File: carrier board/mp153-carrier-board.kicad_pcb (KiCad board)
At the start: 4 copper layers, 66 x 75 mm, 27 parts, among them J3 USB_B_Micro_10118194-0011LF, J4 Socket_02x40_P0.4mm_W3.0mm_SMT, J5 3.5mm_Mono_Switched_sm, J6 Socket_02x40_P0.4mm_W3.0mm_SMT, J7 Eurorack_Power_16pin_Unshroud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, J9 3.5mm_Mono_Switched_sm, U1 TL072H

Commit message: Carrier-board: Added codec and audio in/out
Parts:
- removed J3: USB_B_Micro_10118194-0011LF, Connector_USB:USB_Micro-B_Amphenol_10118194_Horizontal
- added C147: 180pF_0402_25V, 4ms_Capacitor:C_0402, B.Cu at (224.3, 78.4)
- added C148: 180pF_0402_25V, 4ms_Capacitor:C_0402, B.Cu at (229.0, 84.0)
- added C149: 180pF_0402_25V, 4ms_Capacitor:C_0402, B.Cu at (227.2, 74.5)
- added C150: 180pF_0402_25V, 4ms_Capacitor:C_0402, B.Cu at (231.9, 77.4)
- added C152: 820pF_0402_10v, 4ms_Capacitor:C_0402, B.Cu at (226.0, 84.1)
- added C153: 820pF_0402_10v, 4ms_Capacitor:C_0402, B.Cu at (230.1, 73.5)
- added C41: 100nF_0402_16V, 4ms_Capacitor:C_0402, F.Cu at (216.9, 64.9)
- added C42: 220pF_0603_25V, 4ms_Capacitor:C_0603, B.Cu at (217.7, 75.3)
- added C44: 22uF_0805_10V, 4ms_Capacitor:C_0805, F.Cu at (216.1, 67.5)
- added C45: 0.1uF_0603_16V, 4ms_Capacitor:C_0603, F.Cu at (216.1, 69.2)
- added C46: 2.2uF_0603_25V, 4ms_Capacitor:C_0603, B.Cu at (214.7, 82.9)
- added C48: 220pF_0603_25V, 4ms_Capacitor:C_0603, B.Cu at (210.3, 75.9)
- added C49: 2.2uF_0603_25V, 4ms_Capacitor:C_0603, B.Cu at (223.8, 69.4)
- added C51: 10uF_0603_10V, 4ms_Capacitor:C_0603, B.Cu at (223.8, 64.2)
- added C52: 2.2uF_0603_25V, 4ms_Capacitor:C_0603, B.Cu at (212.7, 76.9)
- added C71: 100nF_0402_50V, 4ms_Capacitor:C_0402, B.Cu at (219.9, 79.7)
- added C72: 100nF_0402_50V, 4ms_Capacitor:C_0402, B.Cu at (220.0, 81.7)
- added C75: 100nF_0402_50V, 4ms_Capacitor:C_0402, B.Cu at (212.4, 79.5)
- added C76: 100nF_0402_50V, 4ms_Capacitor:C_0402, B.Cu at (212.4, 82.2)
- added C77: 100nF_0402_50V, 4ms_Capacitor:C_0402, B.Cu at (229.8, 80.5)
- added C78: 100nF_0402_50V, 4ms_Capacitor:C_0402, B.Cu at (229.7, 78.5)
- added J1: USB-C_Receptacle_Molex_2171790001, 4ms_Connector:USB_C_Receptacle_Molex_2171790001, B.Cu at (222.5, 45.6)
- added NT1: NetTie_2, NetTie:NetTie-2_SMD_Pad0.5mm, B.Cu at (224.4, 62.8)
- added R10: 10k_0402, 4ms_Resistor:R_0402, B.Cu at (224.3, 76.2)
- added R14: 10k_0402, 4ms_Resistor:R_0402, B.Cu at (224.4, 77.2)
- added R152: 1k_0402, 4ms_Resistor:R_0402, B.Cu at (224.3, 79.5)
- added R153: 1k_0402, 4ms_Resistor:R_0402, B.Cu at (225.6, 74.1)
- added R157: 24k_0402, 4ms_Resistor:R_0402, B.Cu at (224.3, 80.7)
- added R158: 10k_0402, 4ms_Resistor:R_0402, B.Cu at (227.0, 84.1)
- added R159: 10k_0402, 4ms_Resistor:R_0402, B.Cu at (228.0, 84.0)
- added R160: 24k_0402, 4ms_Resistor:R_0402, B.Cu at (224.4, 84.0)
- added R161: 24k_0402, 4ms_Resistor:R_0402, B.Cu at (227.2, 73.5)
- added R162: 10k_0402, 4ms_Resistor:R_0402, B.Cu at (228.6, 74.1)
- added R163: 10k_0402, 4ms_Resistor:R_0402, B.Cu at (229.7, 76.1)
- added R164: 24k_0402, 4ms_Resistor:R_0402, B.Cu at (230.9, 77.4)
- added R3: 5.1k_0603, 4ms_Resistor:R_0603, F.Cu at (237.5, 83.7)
- added R4: 5.1k_0603, 4ms_Resistor:R_0603, F.Cu at (237.5, 86.2)
- added R42: 14k_0402, 4ms_Resistor:R_0402, B.Cu at (217.1, 74.0)
- added R43: 100k_0402, 4ms_Resistor:R_0402, B.Cu at (215.0, 78.4)
- added R44: 1k_0402, 4ms_Resistor:R_0402, B.Cu at (218.5, 84.7)
- added R47: 4.7k_0402, 4ms_Resistor:R_0402, B.Cu at (210.7, 60.3)
- added R48: 4.7k_0402, 4ms_Resistor:R_0402, B.Cu at (210.7, 59.2)
- added R49: 1M_0402, 4ms_Resistor:R_0402, B.Cu at (216.6, 84.7)
- added R50: 14k_0402, 4ms_Resistor:R_0402, B.Cu at (210.3, 74.5)
- added R51: 100k_0402, 4ms_Resistor:R_0402, B.Cu at (210.2, 73.3)
- added R52: 1k_0402, 4ms_Resistor:R_0402, B.Cu at (211.0, 85.4)
- added R53: 1M_0402, 4ms_Resistor:R_0402, B.Cu at (209.0, 85.4)
- added R54: 1k_0402, 4ms_Resistor:R_0402, B.Cu at (212.2, 73.2)
- added R55: 1k_0402, 4ms_Resistor:R_0402, B.Cu at (217.1, 72.9)
- added R6: 10k_0402, 4ms_Resistor:R_0402, B.Cu at (224.3, 81.9)
- added R7: 10k_0402, 4ms_Resistor:R_0402, B.Cu at (224.3, 83.0)
- added U11: NJM2068, 4ms_Package_SSOP:TSSOP-8_4.4x3mm_Pitch0.65mm, B.Cu at (210.0, 80.7)
- added U12: NJM2068, 4ms_Package_SSOP:TSSOP-8_4.4x3mm_Pitch0.65mm, B.Cu at (227.3, 79.1)
- added U8: NJM2068, 4ms_Package_SSOP:TSSOP-8_4.4x3mm_Pitch0.65mm, B.Cu at (217.4, 80.2)
- added U9: PCM3060PW, Package_SO:TSSOP-28_4.4x9.7mm_P0.65mm, B.Cu at (216.9, 66.1)
- added V1: AP2120N-5.0TRG1, 4ms_Package_SOT:SOT23-3_PO132, B.Cu at (224.1, 66.8)
- renumbered R6 to R8
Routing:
- net GND: track 0.00 -> 125.4 mm, vias 0 -> 15
- net -12VA: track 0.00 -> 36.3 mm, vias 0 -> 5
- net +12V: track 0.00 -> 32.1 mm, vias 0 -> 5
- net +3V3: track 0.00 -> 28.6 mm, vias 0 -> 3
- net GNDA: track 0.00 -> 22.4 mm, vias 0 -> 2
- net /VCOM: track 0.00 -> 21.4 mm, vias 0 -> 5
- net /SAI_FS: track 0.00 -> 20.4 mm, vias 0 -> 1
- net /SAI_SCK: track 0.00 -> 19.5 mm, vias 0 -> 1
- net /SAI_MCLK: track 0.00 -> 17.3 mm, vias 0 -> 1
- net /CODEC_OUT_L+: track 0.00 -> 16.7 mm
- net /CODEC_OUT_L-: track 0.00 -> 16.1 mm
- net /SAI_SD_B: track 0.00 -> 15.7 mm, vias 0 -> 1
- net /D10: track 0.00 -> 15.5 mm, vias 0 -> 1
- net /D17: track 0.00 -> 14.0 mm, vias 0 -> 1
- net /SAI_SD_A: track 0.00 -> 13.6 mm, vias 0 -> 1
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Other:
- board size 66 x 75 mm -> 66 x 78 mm

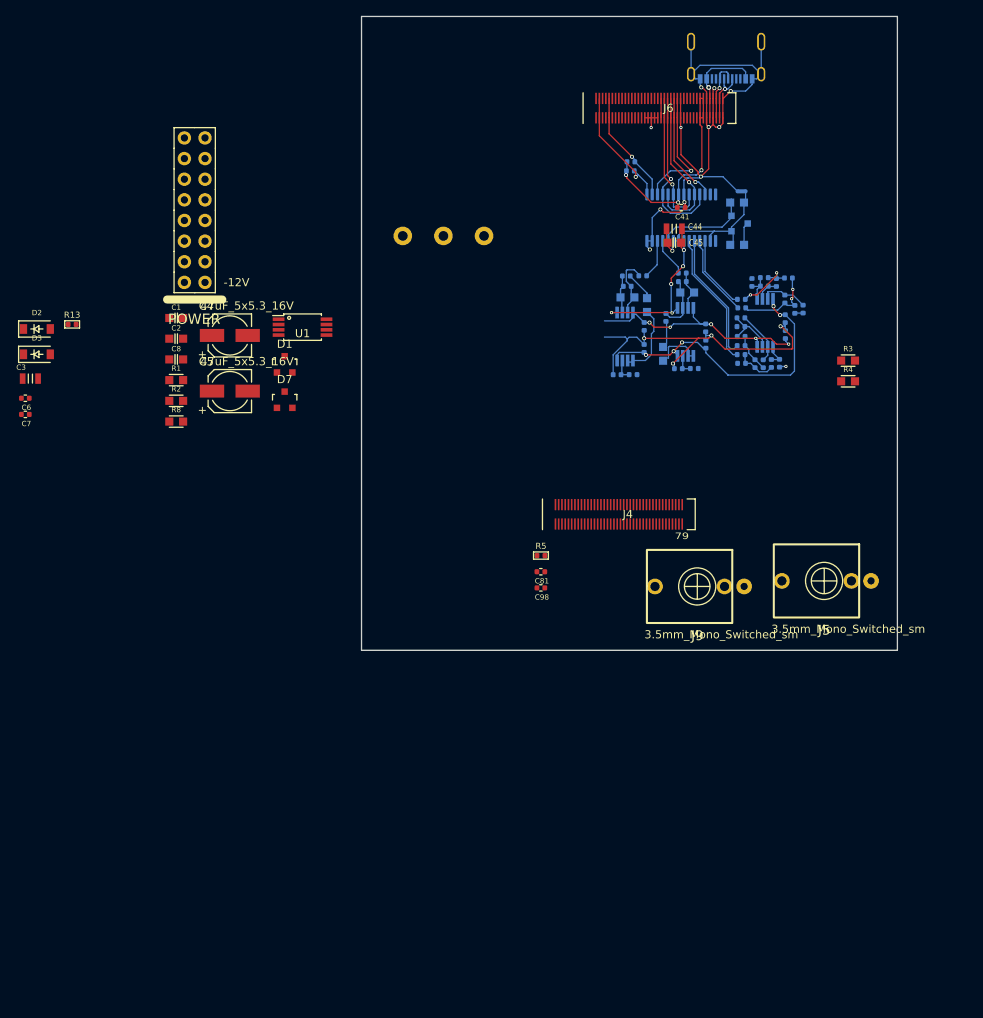
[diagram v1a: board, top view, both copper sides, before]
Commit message: Finished carrier board. Produced JLC files
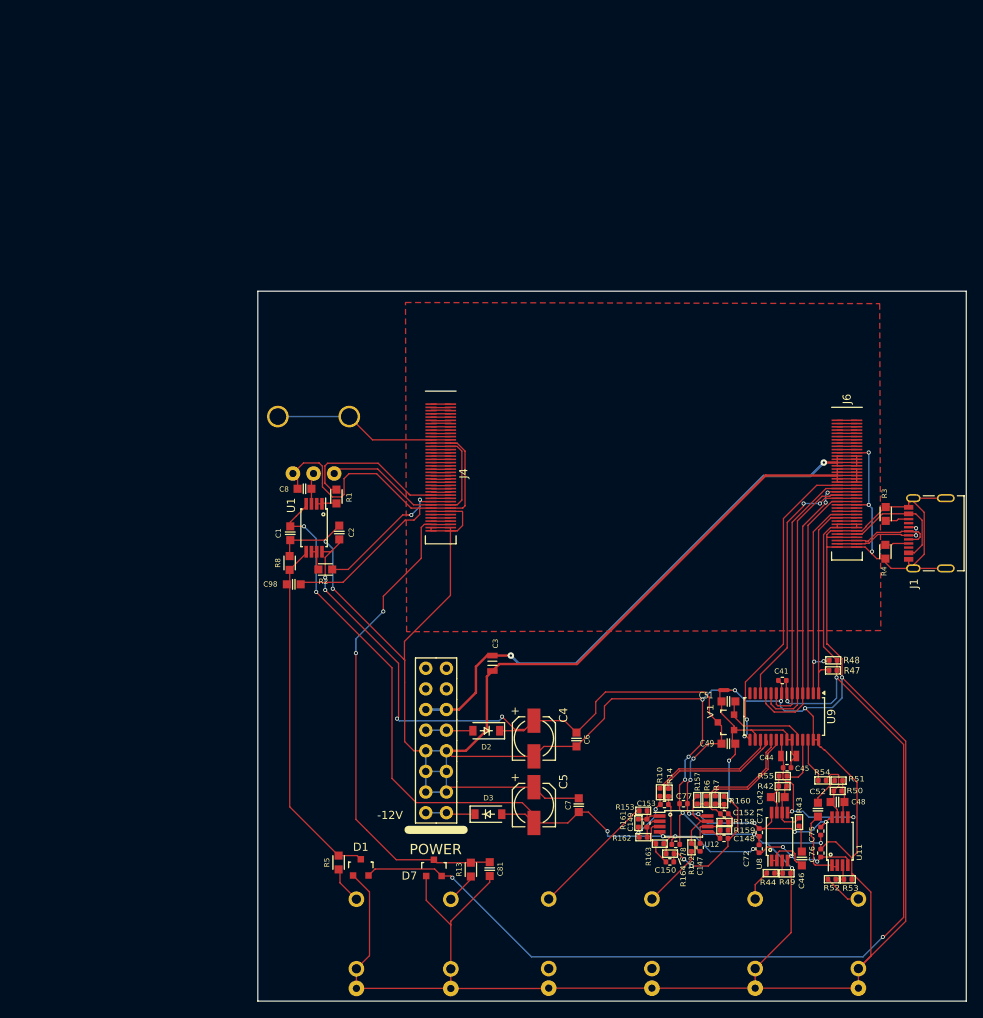
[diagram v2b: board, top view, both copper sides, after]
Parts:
- added J10: 3.5mm_Mono_Switched_sm, 4ms_Jack:EighthInch_PJ398SM, B.Cu at (226.0, 155.2)
- added J11: 3.5mm_Mono_Switched_sm, 4ms_Jack:EighthInch_PJ398SM, B.Cu at (238.7, 155.2)
- added J12: 3.5mm_Mono_Switched_sm, 4ms_Jack:EighthInch_PJ398SM, B.Cu at (200.6, 155.2)
- added J13: 3.5mm_Mono_Switched_sm, 4ms_Jack:EighthInch_PJ398SM, B.Cu at (213.3, 155.2)
- C147, C148, C149, C150, C152, C153, C42, C46, C48, C49, C51, C52, C71, C72, C75, C76, C77, C78, J1, NT1, R10, R14, R152, R153, R157, R158, R159, R160, R161, R162, R163, R164, R42, R43, R44, R47, R48, R49, R50, R51, R52, R53, R54, R55, R6, R7, U9, V1: moved to F.Cu
- C44: value 22uF_0805_10V -> 22uF_0805_25V
- C45: value 0.1uF_0603_16V -> 100nF_0402_16V; footprint 4ms_Capacitor:C_0603 -> 4ms_Capacitor:C_0402
- C6, C7: value 100nF_0402_16V -> 100nF_0603_16V; footprint 4ms_Capacitor:C_0402 -> 4ms_Capacitor:C_0603
- C81, C98: value 10nF_0402_16V -> 10nF_0603_25V; footprint 4ms_Capacitor:C_0402 -> 4ms_Capacitor:C_0603
- J5, J9: moved to B.Cu
- POT1: value 16mm_CtrDet_10k -> 9mm_NoDet_100k_Knurled_Lined; footprint 4ms_Potentiometer:Pot_16mm_CtrDet_RV16AF-4A -> 4ms_Potentiometer:Pot_9mm_Knurl_NoDet
- R1, R2: value 68R_0603 -> 68Ω_0603
- R13, R5: value 47k_0402 -> 47k_0603; footprint 4ms_Resistor:R_0402 -> 4ms_Resistor:R_0603
- U11, U12, U8: value NJM2068 -> TL072H; moved to F.Cu
- moved C7 83.4 mm to (204.3, 138.4), turned to 90 degrees
- moved R13 83.1 mm to (191.0, 146.3), turned to 90 degrees
- moved C6 79.8 mm to (204.0, 130.3), turned to -90 degrees
- moved D3 79.3 mm to (193.2, 139.5)
- moved D2 74.2 mm to (192.9, 129.2), turned to 180 degrees
- moved J5 72.7 mm to (176.9, 155.2), turned to -90 degrees
- moved J7 71.7 mm to (186.8, 130.4)
- moved R162 70.2 mm to (212.3, 142.3), turned to 180 degrees
- moved C150 70.0 mm to (215.5, 145.4), turned to 180 degrees
- moved R161 68.9 mm to (211.7, 140.6), turned to -90 degrees
- moved R163 68.8 mm to (214.3, 143.1), turned to 0 degrees
- moved R164 68.7 mm to (215.6, 144.4), turned to 180 degrees
- moved R53 68.3 mm to (237.4, 147.5), turned to 0 degrees
- moved C149 67.7 mm to (212.7, 140.6), turned to -90 degrees
- moved U11 67.5 mm to (236.5, 142.8)
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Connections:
- net -12VA renamed -12V
- C81 pad 1: /D3 -> /D30
- C98 pad 2: GND -> GNDADC
- D7 pad 3: /D3 -> /D30
- R1 pad 2: /ADC-2 -> /ADC-3
- R13 pad 2: /D3 -> /D30
- R2 pad 2: /ADC-3 -> /ADC-2
- R47 pad 1: /D10 -> /D5
- R48 pad 1: /D17 -> /D21
- U9 pad 1: /D10 -> /D5
- U9 pad 2: /D17 -> /D21
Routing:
- net GND: track 125.4 -> 609.3 mm, vias 15 -> 16
- net +3V3: track 28.6 -> 143.5 mm, vias 3 -> 4
- net +12V: track 32.1 -> 117.5 mm, vias 5 -> 11
- net +5V: track 0.00 -> 78.0 mm, vias 0 -> 2
- net -12V: track 36.3 -> 111.7 mm, vias 5 -> 9
- net GNDADC: track 0.00 -> 61.9 mm
- net /D30: track 0.00 -> 61.7 mm, vias 0 -> 2
- net Net-(D1-AK): track 0.00 -> 43.7 mm
- net /D7: track 2.39 -> 40.5 mm, vias 0 -> 2
- net /D21: track 0.00 -> 28.3 mm, vias 0 -> 2
- net VREF+: track 0.00 -> 28.1 mm
- net /D5: track 0.00 -> 26.8 mm
- net GNDA: track 22.4 -> 44.9 mm, vias 2 -> 4
- net /ADC-3: track 0.00 -> 21.1 mm
- net /SAI_SD_A: track 13.6 -> 32.4 mm, vias 1 -> 2
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- added copper zone on F.Cu, net GND
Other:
- board size 66 x 78 mm -> 87.2 x 87.4 mm
- copper layers 4 -> 2
- board text removed: "79"
